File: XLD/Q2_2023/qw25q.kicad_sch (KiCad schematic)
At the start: 521 parts

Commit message: corrected the names ans the output lines of the opxs
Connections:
- net at EF43.: now also LPF34.; no longer L:96.
- net at EF52.: now also LPF43.; no longer L:104.
- net at EF29.: now also L:5.; no longer LPF20.
- net at EF69.: now also L:153.; no longer LPF60.
- net at Coupler1.: now also L:3.; no longer L:4. (x2)
- net at L:3.: now also TWPA1.; no longer Coupler1.
- net at EF39.: now also LPF30.; no longer L:92.
- net at L:4.: now also Coupler1.; no longer TJI2. (x2)
- net at EF71.: now also LPF62.; no longer L:170.
- net at EF50.: now also L:102.; no longer LPF41.
- net at EF46.: now also L:98.; no longer LPF37.
- net at EF54.: now also L:106.; no longer LPF45.
- net at TJI2.: now also L:4.; no longer L:5.
- net at TWPA1.: now also L:3.; no longer L:2. (x2)
- net at L:3.: now also Coupler1.; no longer TWPA1. (x2)
- net at EF37.: now also L:27.; no longer LPF28.
- net at L:1.: now also TJI1.
- net at TJI1.: now also L:2.; no longer L:1.
- net at L:2.: now also TJI1.; no longer TWPA1. (x2)
- net at TJI1.: now also L:1.; no longer L:2. (x2)
- net at EF70.: now also L:168.; no longer LPF61.
- net at EF33.: now also LPF24.; no longer L:9.
- net at EF31.: now also LPF22.; no longer L:7.
- net at EF64.: now also LPF55.; no longer L:116.
- net at EF27.: now also L:3.; no longer LPF18.
- net at EF62.: now also L:114.; no longer LPF53.
- net at EF68.: now also L:120.; no longer LPF59.
- net at EF66.: now also LPF57.; no longer L:118.
- net at EF41.: now also LPF32.; no longer L:94.
- net at L:4.: now also TJI2.; no longer Coupler1.
- net at EF72.: now also L:174.; no longer LPF63.
- net at L:2.: now also TWPA1.; no longer TJI1.
- net at EF56.: now also L:108.; no longer LPF47.
- net at TJI2.: now also L:5.; no longer L:4.
- net at EF35.: now also L:25.; no longer LPF26.
- net at EF48.: now also L:100.; no longer LPF39.
- net at EF60.: now also LPF51.; no longer L:112.
- net at EF58.: now also LPF49.; no longer L:110.
- new net: EF43., L:96.
- new net: EF52., L:104.
- new net: EF29., LPF20.
- new net: ATT347., ATT348.
- new net: EF69., LPF60.
- new net: Coupler1., L:4. (x2)
- new net: EF39., L:92.
- new net: EF44., LPF35.
- new net: L:4., TJI2.
- new net: EF55., LPF46.
- new net: EF71., L:170.
- new net: EF38., LPF29.
- new net: EF50., LPF41.
- new net: EF46., LPF37.
- new net: EF47., LPF38.
- new net: ATT351., ATT352.
- new net: EF54., LPF45.
- new net: L:5., TJI2.
- new net: L:2., TWPA1. (x3)
- new net: EF37., LPF28.
- new net: EF51., LPF42.
- new net: EF70., LPF61.
- new net: ATT349., ATT350.
- new net: ATT345., ATT346.
- new net: EF65., LPF56.
- new net: EF33., L:9.
- new net: L:6., LX-X2. (x3)
- new net: EF31., L:7.
- new net: EF30., LPF21.
- new net: EF64., L:116.
- new net: EF57., LPF48.
- new net: EF27., LPF18.
- new net: EF49., LPF40.
- new net: EF61., LPF52.
- new net: EF62., LPF53.
- new net: EF68., LPF59.
- new net: EF66., L:118.
- new net: EF41., L:94.
- new net: EF72., LPF63.
- new net: L:2., TJI1.
- new net: EF40., LPF31.
- new net: EF28., LPF19.
- new net: EF56., LPF47.
- new net: EF67., LPF58.
- new net: EF35., LPF26.
- new net: EF63., LPF54.
- new net: EF36., LPF27.
- new net: EF45., LPF36.
- new net: EF53., LPF44.
- new net: EF48., LPF39.
- new net: EF60., L:112.
- new net: EF32., LPF23.
- new net: EF58., L:110.
- new net: EF42., LPF33.
- new net: EF34., LPF25.
- new net: EF59., LPF50.

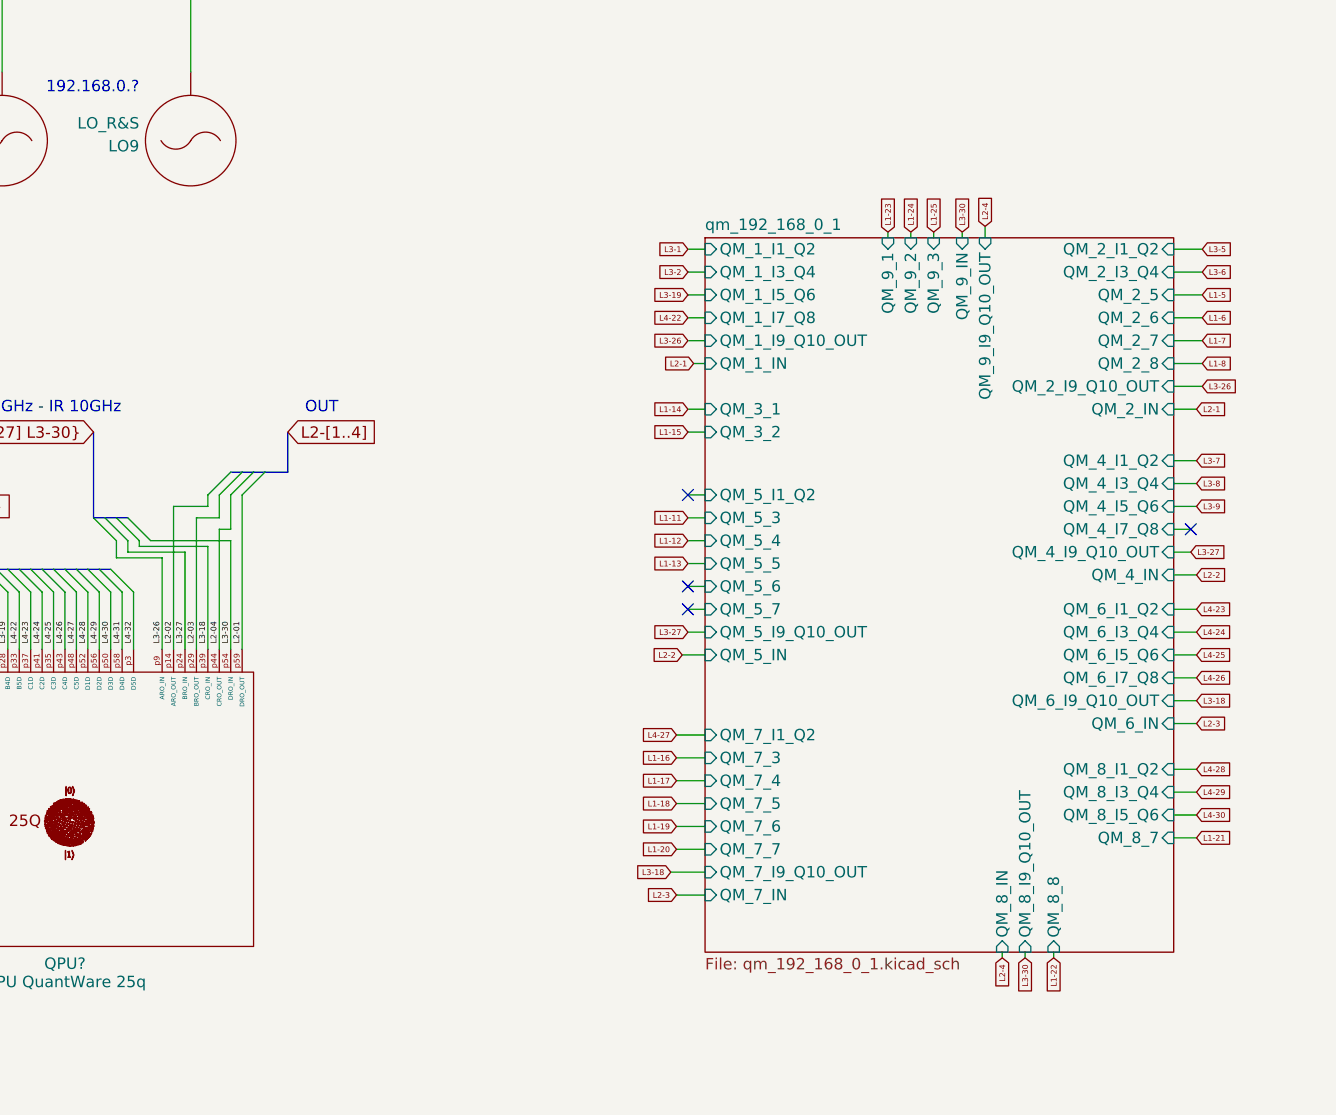
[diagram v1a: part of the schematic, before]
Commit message: add lo oscillators to line b con1 con2 con3
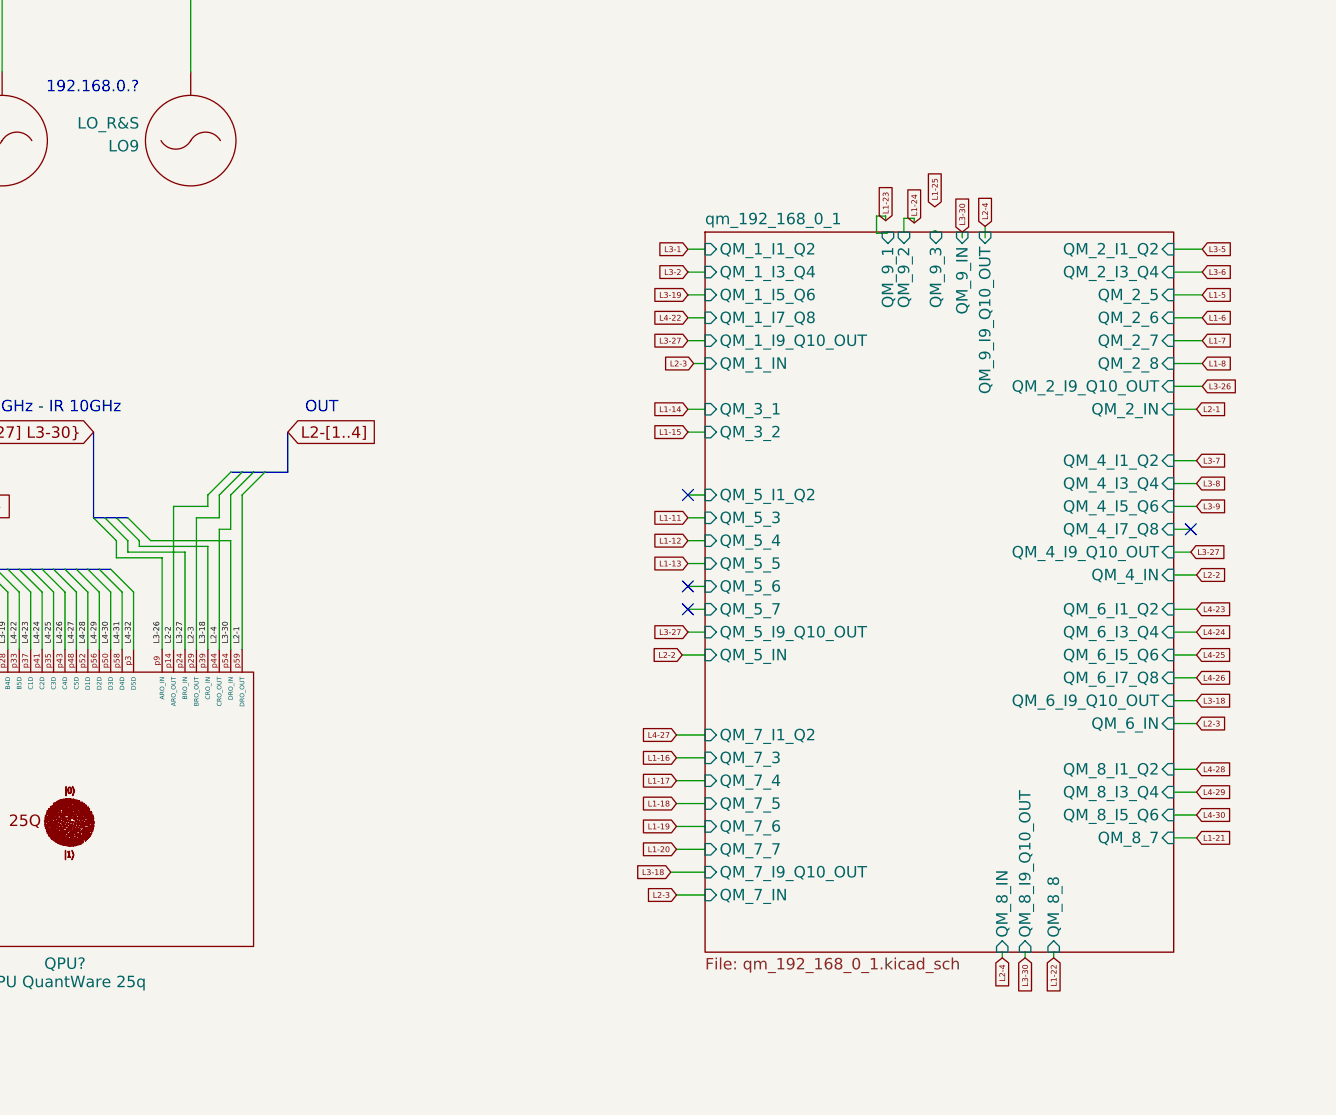
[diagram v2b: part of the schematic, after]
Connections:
- net L2-01 is gone; now on net L2-1: QPU?.p59 (DRO_OUT)
- net L2-02 is gone; now on net L2-2: QPU?.p14 (ARO_OUT)
- net L2-03 is gone; now on net L2-3: QPU?.p29 (BRO_OUT)
- net L2-04 is gone; now on net L2-4: QPU?.p44 (CRO_OUT)
- net at EF43.: now also LPF34.; no longer L:96.
- net at EF52.: now also LPF43.; no longer L:104.
- net at EF29.: now also L:5.; no longer LPF20.
- net at EF69.: now also L:153.; no longer LPF60.
- net at Coupler1.: now also L:3.; no longer L:4. (x2)
- net at L:3.: now also TWPA1.; no longer Coupler1.
- net at EF39.: now also LPF30.; no longer L:92.
- net at L:4.: now also Coupler1.; no longer TJI2. (x2)
- net at EF71.: now also LPF62.; no longer L:170.
- net at EF50.: now also L:102.; no longer LPF41.
- net at EF46.: now also L:98.; no longer LPF37.
- net at EF54.: now also L:106.; no longer LPF45.
- net at TJI2.: now also L:4.; no longer L:5.
- net at TWPA1.: now also L:3.; no longer L:2. (x2)
- net at L:3.: now also Coupler1.; no longer TWPA1. (x2)
- net at EF37.: now also L:27.; no longer LPF28.
- net at L:1.: now also TJI1.
- net at TJI1.: now also L:2.; no longer L:1.
- net at L:2.: now also TJI1.; no longer TWPA1. (x2)
- net at TJI1.: now also L:1.; no longer L:2. (x2)
- net at EF70.: now also L:168.; no longer LPF61.
- net at EF33.: now also LPF24.; no longer L:9.
- net at EF31.: now also LPF22.; no longer L:7.
- net at EF64.: now also LPF55.; no longer L:116.
- net at EF27.: now also L:3.; no longer LPF18.
- net at EF62.: now also L:114.; no longer LPF53.
- net at EF68.: now also L:120.; no longer LPF59.
- net at EF66.: now also LPF57.; no longer L:118.
- net at EF41.: now also LPF32.; no longer L:94.
- net at L:4.: now also TJI2.; no longer Coupler1.
- net at EF72.: now also L:174.; no longer LPF63.
- net at L:2.: now also TWPA1.; no longer TJI1.
- net at EF56.: now also L:108.; no longer LPF47.
- net at TJI2.: now also L:5.; no longer L:4.
- net at EF35.: now also L:25.; no longer LPF26.
- net at EF48.: now also L:100.; no longer LPF39.
- net at EF60.: now also LPF51.; no longer L:112.
- net at EF58.: now also LPF49.; no longer L:110.
- new net: EF43., L:96.
- new net: EF52., L:104.
- new net: EF29., LPF20.
- new net: ATT347., ATT348.
- new net: EF69., LPF60.
- new net: Coupler1., L:4. (x2)
- new net: EF39., L:92.
- new net: EF44., LPF35.
- new net: L:4., TJI2.
- new net: EF55., LPF46.
- new net: EF71., L:170.
- new net: EF38., LPF29.
- new net: EF50., LPF41.
- new net: EF46., LPF37.
- new net: EF47., LPF38.
- new net: ATT351., ATT352.
- new net: EF54., LPF45.
- new net: L:5., TJI2.
- new net: L:2., TWPA1. (x3)
- new net: EF37., LPF28.
- new net: EF51., LPF42.
- new net: EF70., LPF61.
- new net: ATT349., ATT350.
- new net: ATT345., ATT346.
- new net: EF65., LPF56.
- new net: EF33., L:9.
- new net: L:6., LX-X2. (x3)
- new net: EF31., L:7.
- new net: EF30., LPF21.
- new net: EF64., L:116.
- new net: EF57., LPF48.
- new net: EF27., LPF18.
- new net: EF49., LPF40.
- new net: EF61., LPF52.
- new net: EF62., LPF53.
- new net: EF68., LPF59.
- new net: EF66., L:118.
- new net: EF41., L:94.
- new net: EF72., LPF63.
- new net: L:2., TJI1.
- new net: EF40., LPF31.
- new net: EF28., LPF19.
- new net: EF56., LPF47.
- new net: EF67., LPF58.
- new net: EF35., LPF26.
- new net: EF63., LPF54.
- new net: EF36., LPF27.
- new net: EF45., LPF36.
- new net: EF53., LPF44.
- new net: EF48., LPF39.
- new net: EF60., L:112.
- new net: EF32., LPF23.
- new net: EF58., L:110.
- new net: EF42., LPF33.
- new net: EF34., LPF25.
- new net: EF59., LPF50.
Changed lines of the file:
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@@
     (stroke (width 0) (type default))
   )
-  (wire (pts (xy 758.19 402.59) (xy 758.19 403.225))
+  (wire (pts (xy 758.444 402.59) (xy 758.444 402.463))
     (stroke (width 0) (type default))
   )
@@
     (stroke (width 0) (type default))
   )
+  (wire (pts (xy 754.888 401.066) (xy 756.031 401.066))
+    (stroke (width 0) (type default))
+  )
   (wire (pts (xy 533.4 415.29) (xy 533.4 435.61))
     (stroke (width 0) (type default))
@@
     (stroke (width 0) (type default))
   )
+  (wire (pts (xy 751.84 400.812) (xy 751.84 402.717))
+    (stroke (width 0) (type default))
+  )
   (wire (pts (xy 804.545 26.035) (xy 804.545 29.845))
     (stroke (width 0) (type default))
@@
     (stroke (width 0) (type default))
   )
-  (wire (pts (xy 755.65 402.59) (xy 755.65 403.225))
+  (wire (pts (xy 754.888 401.066) (xy 754.888 402.59))
     (stroke (width 0) (type default))
   )
@@
     (stroke (width 0) (type default))
   )
+  (wire (pts (xy 751.84 402.717) (xy 752.983 402.717))
+    (stroke (width 0) (type default))
+  )
   (wire (pts (xy 34.925 396.875) (xy 34.925 402.59))
     (stroke (width 0) (type default))
@@
     (stroke (width 0) (type default))
   )
-  (wire (pts (xy 753.11 402.59) (xy 753.11 403.225))
+  (wire (pts (xy 753.11 402.59) (xy 752.983 402.717))
     (stroke (width 0) (type default))
   )
@@
     (stroke (width 0) (type default))
   )
+  (wire (pts (xy 758.444 402.463) (xy 758.19 402.463))
+    (stroke (width 0) (type default))
+  )
   (wire (pts (xy 436.88 396.24) (xy 436.88 401.955))
     (stroke (width 0) (type default))
@@
     (stroke (width 0) (type default))
   )
+  (wire (pts (xy 751.84 400.812) (xy 752.856 400.812))
+    (stroke (width 0) (type default))
+  )
   (wire (pts (xy 627.38 135.89) (xy 627.38 142.875))
     (stroke (width 0) (type default))
@@
     (stroke (width 0) (type default))
   )
+  (wire (pts (xy 756.031 401.066) (xy 756.031 401.574))
+    (stroke (width 0) (type default))
+  )
   (bus (pts (xy 654.05 440.055) (xy 655.32 440.055))
     (stroke (width 0) (type default))
@@
     (stroke (width 0) (type default))
   )
+  (wire (pts (xy 752.856 400.812) (xy 752.856 401.32))
+    (stroke (width 0) (type default))
+  )
   (wire (pts (xy 784.86 438.15) (xy 786.765 438.15))
     (stroke (width 0) (type default))
@@
     (effects (font (size 1.27 1.27)) (justify left bottom))
   )
-  (label "L2-01" (at 681.355 448.31 90) (fields_autoplaced)
+  (label "L2-1" (at 681.355 448.31 90) (fields_autoplaced)
     (effects (font (size 0.64 0.64)) (justify left bottom))
   )
@@
     (effects (font (size 1.27 1.27)) (justify left bottom))
   )
-  (label "L2-02" (at 673.735 448.31 90) (fields_autoplaced)
+  (label "L2-2" (at 673.735 448.31 90) (fields_autoplaced)
     (effects (font (size 0.64 0.64)) (justify left bottom))
   )
@@
     (effects (font (size 1.27 1.27)) (justify left bottom))
   )
-  (label "L2-03" (at 676.275 448.31 90) (fields_autoplaced)
+  (label "L2-3" (at 676.275 448.31 90) (fields_autoplaced)
     (effects (font (size 0.64 0.64)) (justify left bottom))
   )
@@
     (effects (font (size 1.27 1.27)) (justify left bottom))
   )
-  (label "L2-04" (at 678.815 448.31 90) (fields_autoplaced)
+  (label "L2-4" (at 678.815 448.31 90) (fields_autoplaced)
     (effects (font (size 0.64 0.64)) (justify left bottom))
   )
@@
     )
   )
-  (global_label "L1-25" (shape input) (at 758.19 402.59 90) (fields_autoplaced)
+  (global_label "L1-25" (shape input) (at 758.317 399.796 90) (fields_autoplaced)
     (effects (font (size 0.64 0.64)) (justify left))
-    (property "Intersheetrefs" "${INTERSHEET_REFS}" (at 758.19 397.9867 90)
+    (property "Intersheetrefs" "${INTERSHEET_REFS}" (at 758.317 395.1927 90)
       (effects (font (size 1.27 1.27)) (justify left) hide)
     )
@@
     )
   )
-  (global_label "L2-1" (shape input) (at 731.52 417.195 180) (fields_autoplaced)
+  (global_label "L2-3" (shape input) (at 731.52 417.195 180) (fields_autoplaced)
     (effects (font (size 0.64 0.64)) (justify right))
     (property "Intersheetrefs" "${INTERSHEET_REFS}" (at 727.5262 417.195 0)
@@
     )
   )
-  (global_label "L3-26" (shape input) (at 730.885 414.655 180) (fields_autoplaced)
+  (global_label "L3-27" (shape input) (at 730.885 414.655 180) (fields_autoplaced)
     (effects (font (size 0.64 0.64)) (justify right))
     (property "Intersheetrefs" "${INTERSHEET_REFS}" (at 726.2817 414.655 0)
@@
     )
   )
-  (global_label "L1-23" (shape input) (at 753.11 402.59 90) (fields_autoplaced)
+  (global_label "L1-23" (shape input) (at 752.856 401.32 90) (fields_autoplaced)
     (effects (font (size 0.64 0.64)) (justify left))
-    (property "Intersheetrefs" "${INTERSHEET_REFS}" (at 753.11 397.9867 90)
+    (property "Intersheetrefs" "${INTERSHEET_REFS}" (at 752.856 396.7167 90)
       (effects (font (size 1.27 1.27)) (justify left) hide)
     )
@@
     )
   )
-  (global_label "L1-24" (shape input) (at 755.65 402.59 90) (fields_autoplaced)
+  (global_label "L1-24" (shape input) (at 756.031 401.574 90) (fields_autoplaced)
     (effects (font (size 0.64 0.64)) (justify left))
-    (property "Intersheetrefs" "${INTERSHEET_REFS}" (at 755.65 397.9867 90)
+    (property "Intersheetrefs" "${INTERSHEET_REFS}" (at 756.031 396.9707 90)
       (effects (font (size 1.27 1.27)) (justify left) hide)
     )
@@
     )
   )
-  (sheet (at 732.79 403.225) (size 52.07 79.375) (fields_autoplaced)
+  (sheet (at 732.79 402.59) (size 52.07 80.01) (fields_autoplaced)
     (stroke (width 0.1524) (type solid))
     (fill (color 0 0 0 0.0000))
-    (property "Sheetname" "qm_192_168_0_1" (at 732.79 402.5134 0)
+    (property "Sheetname" "qm_192_168_0_1" (at 732.79 401.8784 0)
       (effects (font (size 1.27 1.27)) (justify left bottom))
     )
@@
       (effects (font (size 1.27 1.27)) (justify right))
     )
-    (pin "QM_9_3" input (at 758.19 403.225 90)
+    (pin "QM_9_3" input (at 758.444 402.59 90)
       (effects (font (size 1.27 1.27)) (justify right))
     )
-    (pin "QM_9_1" input (at 753.11 403.225 90)
+    (pin "QM_9_1" input (at 753.11 402.59 90)
       (effects (font (size 1.27 1.27)) (justify right))
     )
-    (pin "QM_9_2" input (at 755.65 403.225 90)
+    (pin "QM_9_2" input (at 754.888 402.59 90)
       (effects (font (size 1.27 1.27)) (justify right))
     )
@@
       (effects (font (size 1.27 1.27)) (justify left))
     )
-    (pin "QM_9_IN" input (at 761.365 403.225 90)
+    (pin "QM_9_IN" input (at 761.365 402.59 90)
       (effects (font (size 1.27 1.27)) (justify right))
     )
-    (pin "QM_9_I9_Q10_OUT" input (at 763.905 403.225 90)
+    (pin "QM_9_I9_Q10_OUT" input (at 763.905 402.59 90)
       (effects (font (size 1.27 1.27)) (justify right))
     )

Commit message: partial re-labeling
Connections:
- net at EF43.: now also LPF34.; no longer L:96.
- net at EF52.: now also LPF43.; no longer L:104.
- net at EF29.: now also L:5.; no longer LPF20.
- net at EF69.: now also L:153.; no longer LPF60.
- net at Coupler1.: now also L:3.; no longer L:4. (x2)
- net at L:3.: now also TWPA1.; no longer Coupler1.
- net at EF39.: now also LPF30.; no longer L:92.
- net at L:4.: now also Coupler1.; no longer TJI2. (x2)
- net at EF71.: now also LPF62.; no longer L:170.
- net at EF50.: now also L:102.; no longer LPF41.
- net at EF46.: now also L:98.; no longer LPF37.
- net at EF54.: now also L:106.; no longer LPF45.
- net at TJI2.: now also L:4.; no longer L:5.
- net at TWPA1.: now also L:3.; no longer L:2. (x2)
- net at L:3.: now also Coupler1.; no longer TWPA1. (x2)
- net at EF37.: now also L:27.; no longer LPF28.
- net at L:1.: now also TJI1.
- net at TJI1.: now also L:2.; no longer L:1.
- net at L:2.: now also TJI1.; no longer TWPA1. (x2)
- net at TJI1.: now also L:1.; no longer L:2. (x2)
- net at EF70.: now also L:168.; no longer LPF61.
- net at EF33.: now also LPF24.; no longer L:9.
- net at EF31.: now also LPF22.; no longer L:7.
- net at EF64.: now also LPF55.; no longer L:116.
- net at EF27.: now also L:3.; no longer LPF18.
- net at EF62.: now also L:114.; no longer LPF53.
- net at EF68.: now also L:120.; no longer LPF59.
- net at EF66.: now also LPF57.; no longer L:118.
- net at EF41.: now also LPF32.; no longer L:94.
- net at L:4.: now also TJI2.; no longer Coupler1.
- net at EF72.: now also L:174.; no longer LPF63.
- net at L:2.: now also TWPA1.; no longer TJI1.
- net at EF56.: now also L:108.; no longer LPF47.
- net at TJI2.: now also L:5.; no longer L:4.
- net at EF35.: now also L:25.; no longer LPF26.
- net at EF48.: now also L:100.; no longer LPF39.
- net at EF60.: now also LPF51.; no longer L:112.
- net at EF58.: now also LPF49.; no longer L:110.
- new net: EF43., L:96.
- new net: EF52., L:104.
- new net: EF29., LPF20.
- new net: ATT347., ATT348.
- new net: EF69., LPF60.
- new net: Coupler1., L:4. (x2)
- new net: EF39., L:92.
- new net: EF44., LPF35.
- new net: L:4., TJI2.
- new net: EF55., LPF46.
- new net: EF71., L:170.
- new net: EF38., LPF29.
- new net: EF50., LPF41.
- new net: EF46., LPF37.
- new net: EF47., LPF38.
- new net: ATT351., ATT352.
- new net: EF54., LPF45.
- new net: L:5., TJI2.
- new net: L:2., TWPA1. (x3)
- new net: EF37., LPF28.
- new net: EF51., LPF42.
- new net: EF70., LPF61.
- new net: ATT349., ATT350.
- new net: ATT345., ATT346.
- new net: EF65., LPF56.
- new net: EF33., L:9.
- new net: L:6., LX-X2. (x3)
- new net: EF31., L:7.
- new net: EF30., LPF21.
- new net: EF64., L:116.
- new net: EF57., LPF48.
- new net: EF27., LPF18.
- new net: EF49., LPF40.
- new net: EF61., LPF52.
- new net: EF62., LPF53.
- new net: EF68., LPF59.
- new net: EF66., L:118.
- new net: EF41., L:94.
- new net: EF72., LPF63.
- new net: L:2., TJI1.
- new net: EF40., LPF31.
- new net: EF28., LPF19.
- new net: EF56., LPF47.
- new net: EF67., LPF58.
- new net: EF35., LPF26.
- new net: EF63., LPF54.
- new net: EF36., LPF27.
- new net: EF45., LPF36.
- new net: EF53., LPF44.
- new net: EF48., LPF39.
- new net: EF60., L:112.
- new net: EF32., LPF23.
- new net: EF58., L:110.
- new net: EF42., LPF33.
- new net: EF34., LPF25.
- new net: EF59., LPF50.
